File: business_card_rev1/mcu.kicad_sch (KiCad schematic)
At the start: 11 parts, among them J1 Conn_02x05_Counter_Clockwise, SW1 SW_Push, U1 STM32L031F6P6, X1 MU00525-32.768K

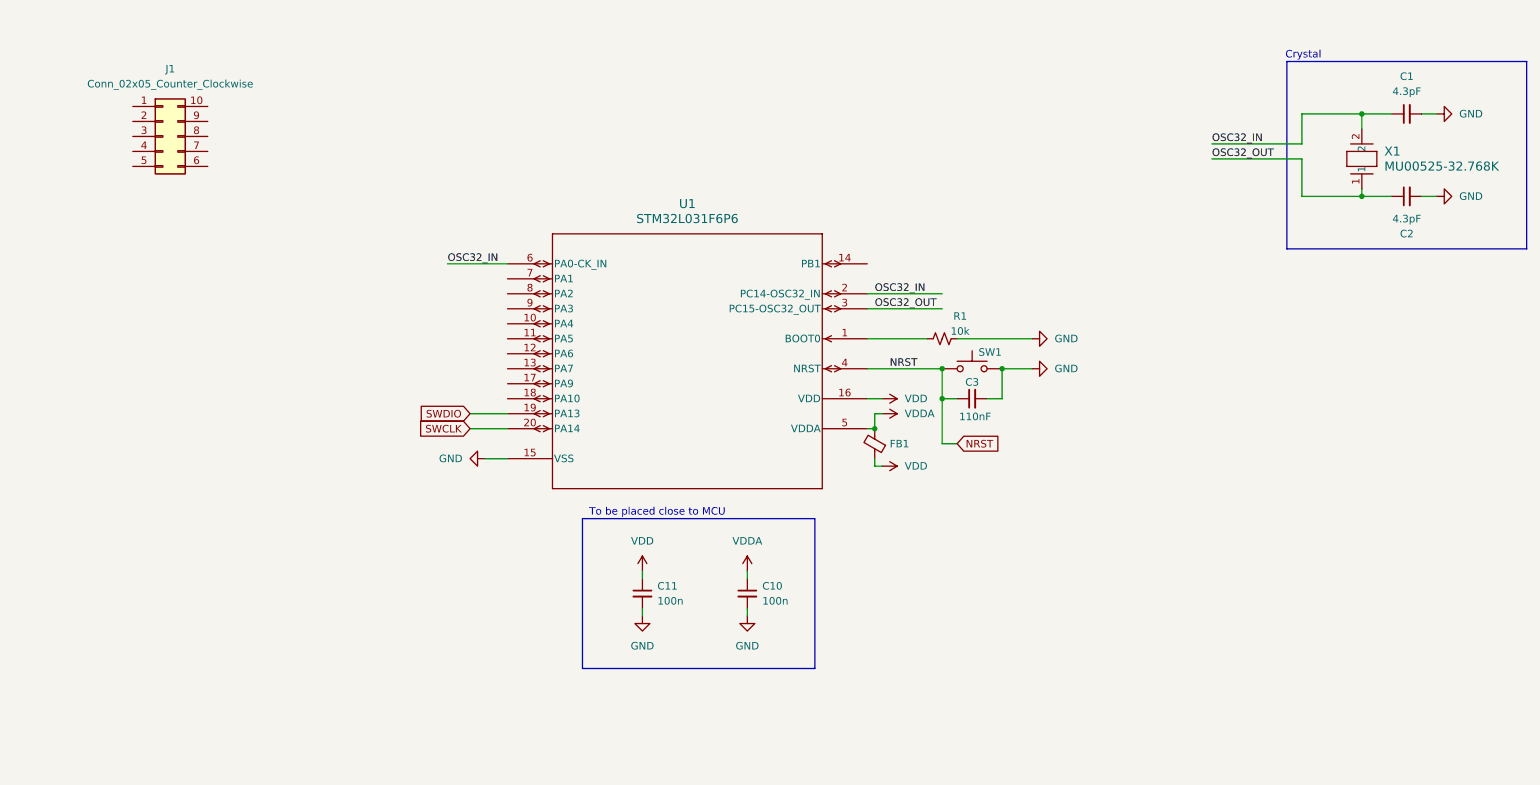
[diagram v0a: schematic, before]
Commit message: Fleshed-out basic schematic and set-up STM32CubeIDE.
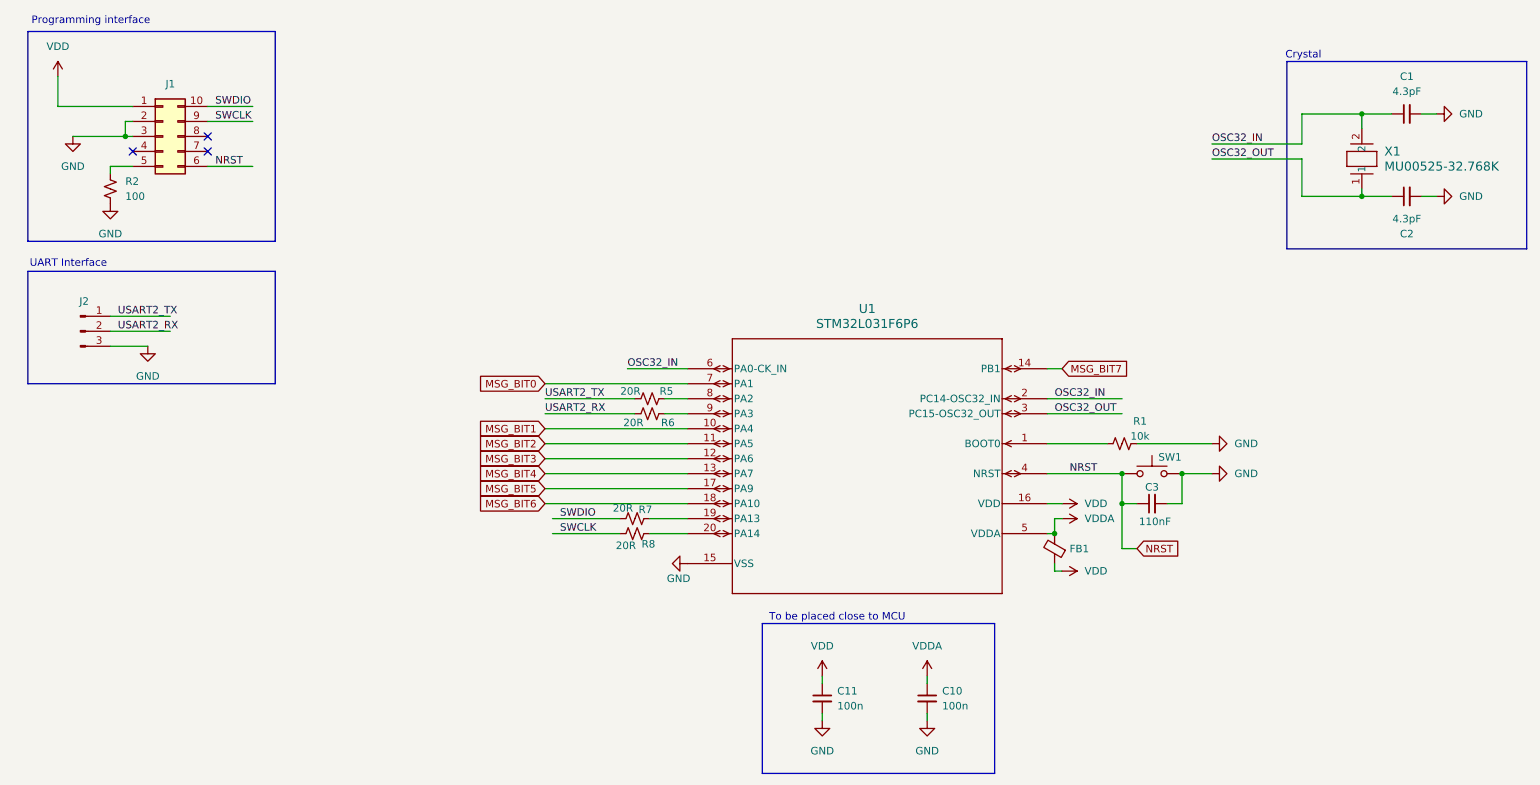
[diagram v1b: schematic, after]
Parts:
- added J2: Conn_01x03_Pin, symbol Connector:Conn_01x03_Pin
- added R2: 100, symbol Device:R_Small_US
- added R5, R6, R7, R8: 20R, symbol Device:R_Small_US
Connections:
- net GND: now also J1.2 (Pin_2), J1.3 (Pin_3), J2.3 (Pin_3), R2.2
- net NRST: now also J1.6 (Pin_6)
- net SWCLK: now also J1.9 (Pin_9), R8.1; no longer U1.20 (PA14)
- net SWDIO: now also J1.10 (Pin_10), R7.1; no longer U1.19 (PA13)
- net VDD: now also J1.1 (Pin_1)
- net MSG_BIT1: now reaches U1.10 (PA4)
- net MSG_BIT2: now reaches U1.11 (PA5)
- net MSG_BIT3: now reaches U1.12 (PA6)
- net MSG_BIT4: now reaches U1.13 (PA7)
- net MSG_BIT7: now reaches U1.14 (PB1)
- net MSG_BIT5: now reaches U1.17 (PA9)
- net MSG_BIT6: now reaches U1.18 (PA10)
- net MSG_BIT0: now reaches U1.7 (PA1)
- net at U1.8 (PA2): now also R5.2
- net at U1.9 (PA3): now also R6.2
- net at J1.5 (Pin_5): now also R2.1
- new net: R8.2, U1.20 (PA14)
- new net: R7.2, U1.19 (PA13)
- new net USART2_RX: J2.2 (Pin_2), R6.1
- new net USART2_TX: J2.1 (Pin_1), R5.1
- no-connect marks 0 -> 3
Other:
- note added: "Programming interface"
- note added: "UART Interface"
- moved on the sheet: C10, C11, C3, FB1, R1, SW1, U1

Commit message: Chose components and drafted rough PCB layout.
Need to check schematic and clean up layout.
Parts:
- removed C10: 100n, symbol Device:C_Small
- removed R5, R6, R7: 20R, symbol Device:R_Small_US
- removed SW1: SW_Push, symbol Switch:SW_Push
- added C12: 100n, Capacitor_SMD:C_0402_1005Metric, symbol Device:C_Small
- added R16, R17, R18: 20R, Resistor_SMD:R_0402_1005Metric, symbol Device:R_Small_US
- added U3: PTS645SM43SMTR92LFS, SWITCH_43SMTR92LFS, symbol PTS645SM43SMTR92LFS:PTS645SM43SMTR92LFS
- C1, C11, C2, C3: footprint (none) -> Capacitor_SMD:C_0402_1005Metric
- FB1, R1, R2: footprint (none) -> Resistor_SMD:R_0603_1608Metric
- J1: footprint (none) -> Connector_PinHeader_1.00mm:PinHeader_2x05_P1.00mm_Vertical
- J2: footprint (none) -> Connector_PinHeader_1.00mm:PinHeader_1x03_P1.00mm_Vertical
- R8: footprint (none) -> Resistor_SMD:R_0402_1005Metric
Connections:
- net GND: now also C12.2, U3.3
- net NRST: now also U3.1
- net SWDIO: now also R16.1
- net USART2_RX: now also R17.1
- net USART2_TX: now also R18.1
- net VDDA: now also C12.1
- net at U1.19 (PA13): now also R16.2
- net at U1.8 (PA2): now also R18.2
- net at U1.9 (PA3): now also R17.2
- no-connect marks 3 -> 5

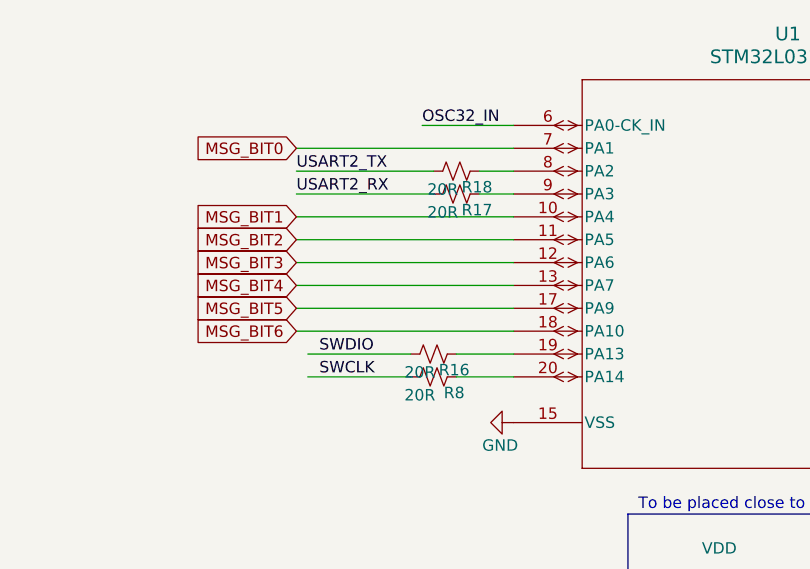
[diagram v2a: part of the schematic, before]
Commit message: Completed layout V1.
Need to review schematic and layout and verify component selection.
Need to add silkscreen info.
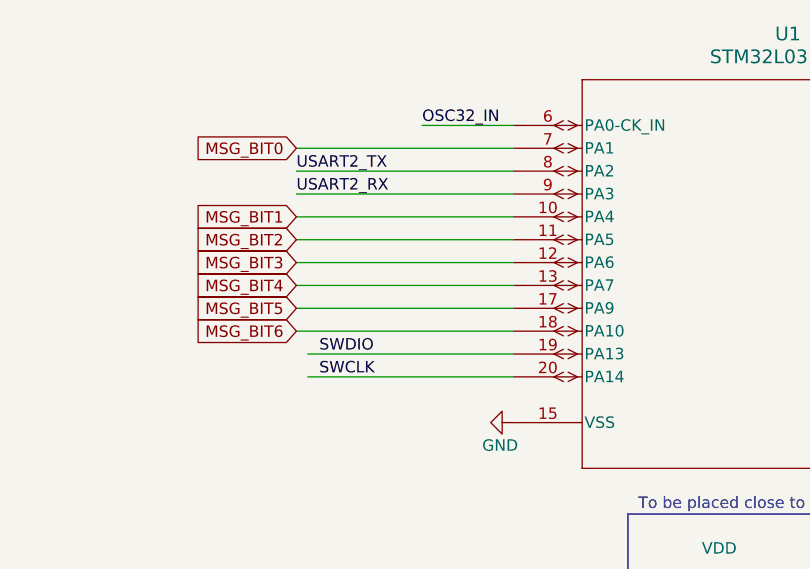
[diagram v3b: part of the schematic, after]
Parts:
- removed R16, R17, R18, R8: 20R, Resistor_SMD:R_0402_1005Metric, symbol Device:R_Small_US
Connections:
- net SWCLK: now also U1.20 (PA14)
- net SWDIO: now also U1.19 (PA13)
- net USART2_RX: now also U1.9 (PA3)
- net USART2_TX: now also U1.8 (PA2)

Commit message: [HW] Edits to PCB design and added QR codes.
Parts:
- removed J1: Conn_02x05_Counter_Clockwise, Connector_PinHeader_1.00mm:PinHeader_2x05_P1.00mm_Vertical, symbol Connector_Generic:Conn_02x05_Counter_Clockwise
- removed R2: 100, Resistor_SMD:R_0603_1608Metric, symbol Device:R_Small_US
- added C13: 100n, Capacitor_SMD:C_0402_1005Metric, symbol Device:C_Small
- added J3: Conn_01x05_Pin, Connector_PinHeader_1.00mm:PinHeader_1x05_P1.00mm_Vertical, symbol Connector:Conn_01x05_Pin
- added R5: 10k, Resistor_SMD:R_0603_1608Metric, symbol Device:R_Small_US
- C11: value 100n -> 1u
- C3: value 110nF -> 100n
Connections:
- net GND: now also C13.2, J3.5 (Pin_5)
- net NRST: now also J3.4 (Pin_4), R5.1
- net SWCLK: now also J3.3 (Pin_3)
- net SWDIO: now also J3.2 (Pin_2)
- net VDD: now also C13.1, J3.1 (Pin_1), R5.2
- no-connect marks 5 -> 2
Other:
- moved on the sheet: C11, C3, R1
